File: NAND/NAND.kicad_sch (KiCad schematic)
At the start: 7 parts, among them J1 5-146280-3-ND, J2 5-146280-3-ND, Q1 DMP2004K-7, Q2 DMP2004K-7

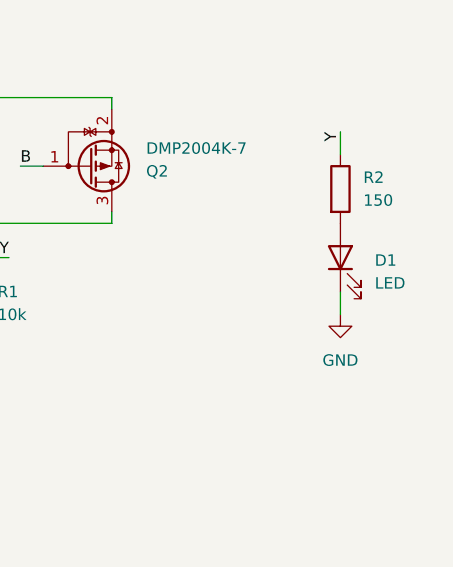
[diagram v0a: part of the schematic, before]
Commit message: Finish NOR gate PCB and unify NAND with it
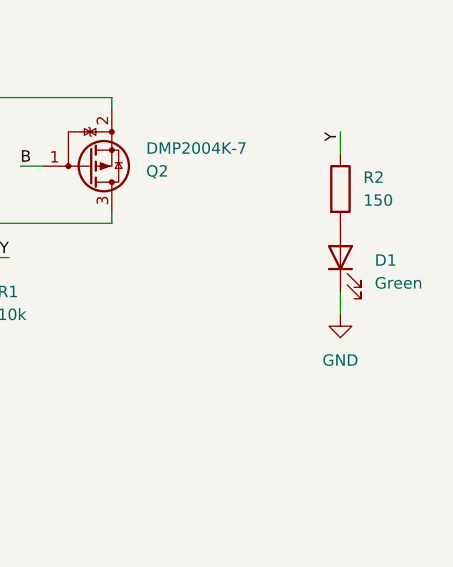
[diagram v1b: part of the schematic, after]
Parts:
- D1: value LED -> Green
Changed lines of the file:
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@@
 			)
 		)
-		(property "Value" "LED"
+		(property "Value" "Green"
 			(at 194.31 115.8874 90)
 			(effects
